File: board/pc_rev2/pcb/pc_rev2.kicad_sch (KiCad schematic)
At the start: 22 parts, among them J1 Conn_02x13_Odd_Even, J10 Conn_01x05, J11 Conn_01x03, J14 Conn_01x03, J2 Conn_02x08_Row_Letter_Last, J20 Conn_01x03, J3 Conn_02x06_Row_Letter_Last, J4 Conn_02x10_Row_Letter_Last, J5 Conn_Grove_Host, J6 Conn_01x03, J7 Conn_01x03, J8 Conn_Grove-Analog_Host, J9 Conn_Grove-Analog_Host, U2 SKU2782

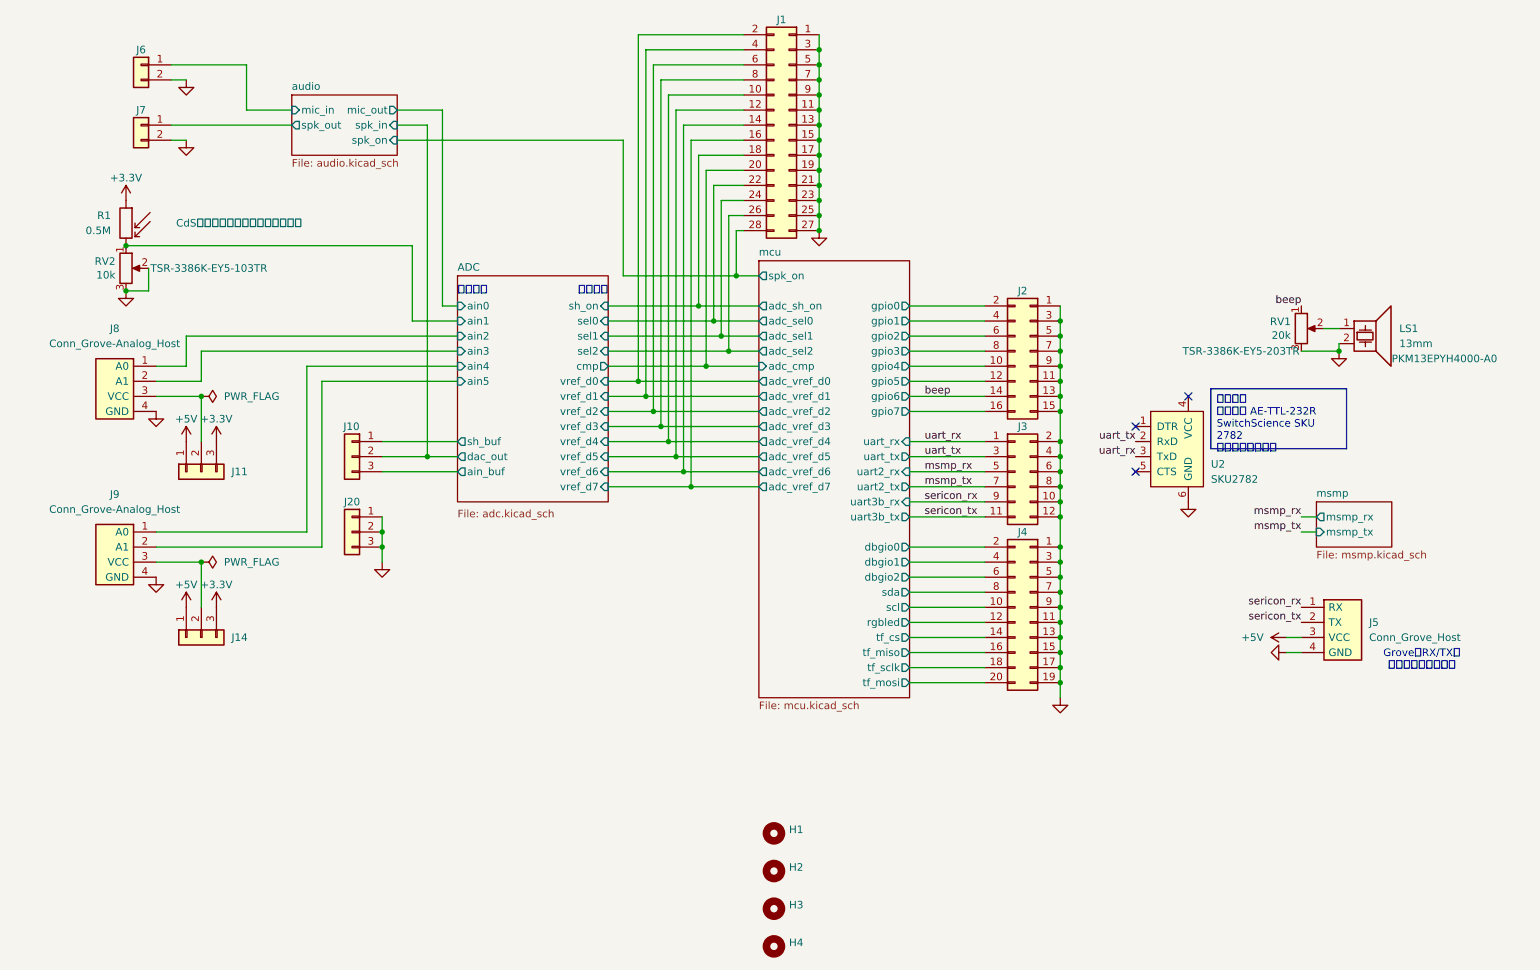
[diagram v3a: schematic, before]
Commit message: I2C用Groveコネクタを追加
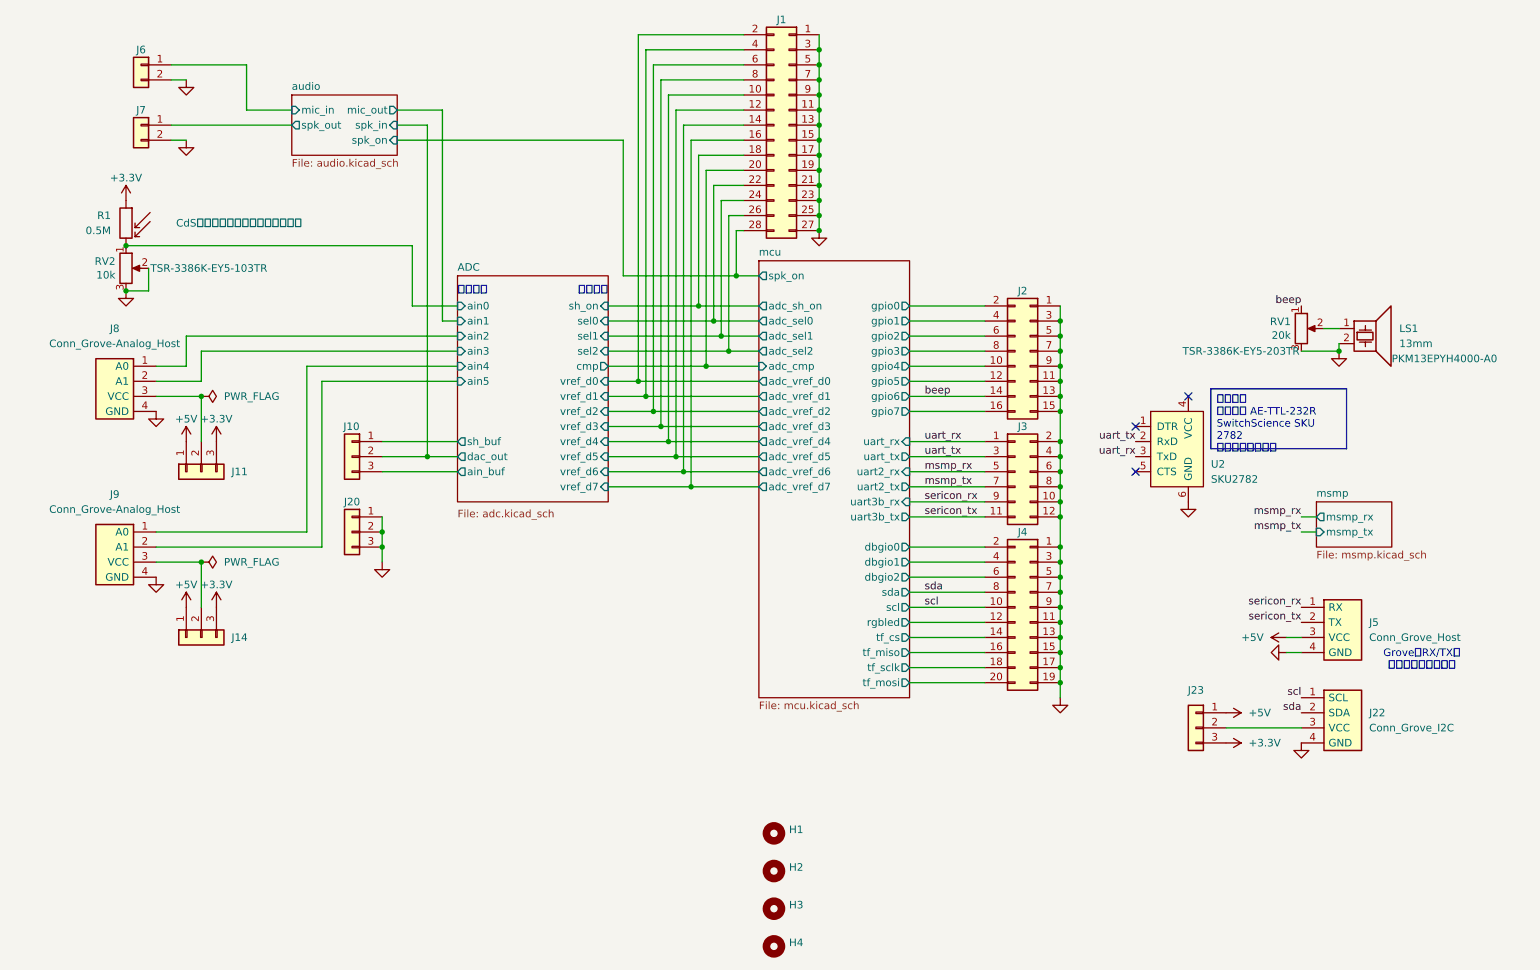
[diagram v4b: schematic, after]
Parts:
- added J22: Conn_Grove_I2C, uchan:Grove_1x04_P2mm_THT_Horizontal, symbol uchan:Conn_Grove_I2C
- added J23: Conn_01x03, Connector_PinHeader_2.54mm:PinHeader_1x03_P2.54mm_Vertical, symbol Connector_Generic:Conn_01x03
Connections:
- net +3.3V: now also J23.3 (Pin_3)
- net +5V: now also J23.1 (Pin_1)
- net ADC/ain0: now also R1.2, RV2.1
- net ADC/ain1: no longer R1.2, RV2.1
- net GND: now also J22.4 (GND)
- net mcu/scl renamed scl
- net scl: now also J22.1 (SCL)
- net mcu/sda renamed sda
- net sda: now also J22.2 (SDA)
- new net: J22.3 (VCC), J23.2 (Pin_2)
